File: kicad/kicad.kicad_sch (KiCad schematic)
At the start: 9 parts, among them SW101 PWR_SWITCH

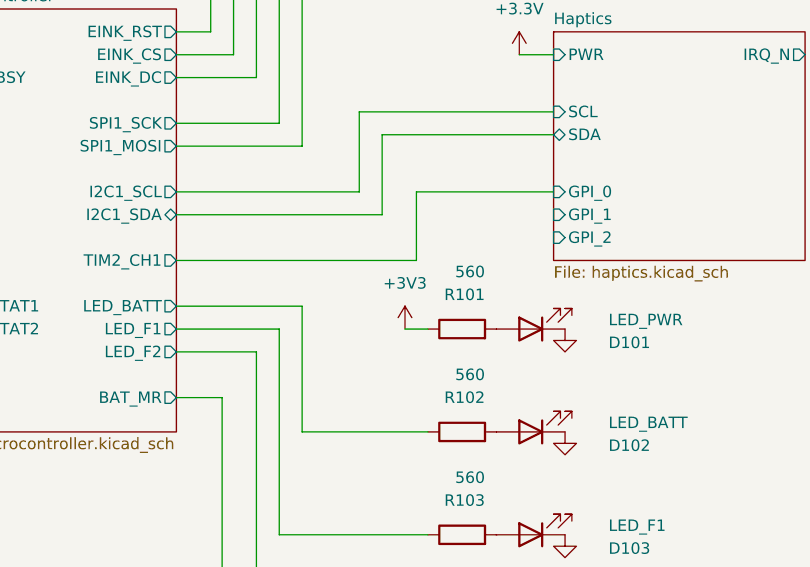
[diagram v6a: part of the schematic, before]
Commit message: PCB Trace progress
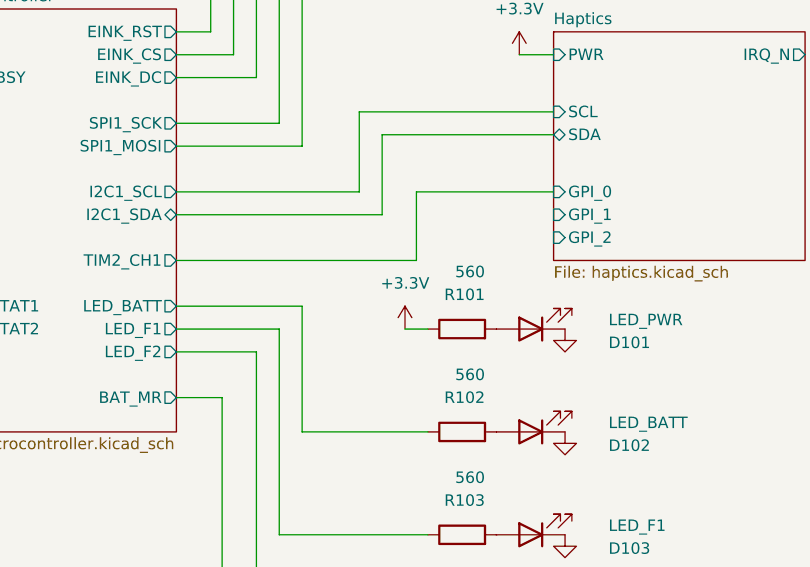
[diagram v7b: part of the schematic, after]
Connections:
- net +3V3 is gone; now on net +3.3V: R101.1
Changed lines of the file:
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@@
-	)
-	(symbol
-		(lib_id "power:+3V3")
-		(at 172.72 114.3 0)
-		(unit 1)
-		(exclude_from_sim no)
-		(in_bom yes)
-		(on_board yes)
-		(dnp no)
-		(fields_autoplaced yes)
-		(property "Reference" "#PWR0111"
-			(at 172.72 118.11 0)
-			(effects
-				(font
-					(size 1.27 1.27)
-				)
-				(hide yes)
-			)
-		)
-		(property "Value" "+3V3"
-			(at 172.72 109.22 0)
-			(effects
-				(font
-					(size 1.27 1.27)
-				)
-			)
-		)
-		(property "Footprint" ""
-			(at 172.72 114.3 0)
-			(effects
-				(font
-					(size 1.27 1.27)
-				)
-				(hide yes)
-			)
-		)
-		(property "Datasheet" ""
-			(at 172.72 114.3 0)
-			(effects
-				(font
-					(size 1.27 1.27)
-				)
-				(hide yes)
-			)
-		)
-		(property "Description" "Power symbol creates a global label with name \"+3V3\""
-			(at 172.72 114.3 0)
-			(effects
-				(font
-					(size 1.27 1.27)
-				)
-				(hide yes)
-			)
-		)
-		(pin "1"
-		)
-		(instances
-			(project "kicad"
-				(path "/97e37379-fec6-4f0d-82d9-4ea53516bb02"
-					(reference "#PWR0111")
-					(unit 1)
-				)
-			)
-		)
 	)
 	(symbol
@@
 					(unit 1)
 				)
+			)
+		)
+	)
+	(symbol
+		(lib_id "power:+3.3V")
+		(at 172.72 114.3 0)
+		(unit 1)
+		(exclude_from_sim no)
+		(in_bom yes)
+		(on_board yes)
+		(dnp no)
+		(fields_autoplaced yes)
+		(property "Reference" "#PWR0111"
+			(at 172.72 118.11 0)
+			(effects
+				(font
+					(size 1.27 1.27)
+				)
+				(hide yes)
+			)
+		)
+		(property "Value" "+3.3V"
+			(at 172.72 109.22 0)
+			(effects
+				(font
+					(size 1.27 1.27)
+				)
+			)
+		)
+		(property "Footprint" ""
+			(at 172.72 114.3 0)
+			(effects
+				(font
+					(size 1.27 1.27)
+				)
+				(hide yes)
+			)
+		)
+		(property "Datasheet" ""
+			(at 172.72 114.3 0)
+			(effects
+				(font
+					(size 1.27 1.27)
+				)
+				(hide yes)
+			)
+		)
+		(property "Description" "Power symbol creates a global label with name \"+3.3V\""
+			(at 172.72 114.3 0)
+			(effects
+				(font
+					(size 1.27 1.27)
+				)
+				(hide yes)
+			)
+		)
+		(pin "1"
+		)
+		(instances
+			(project "kicad"
+				(path "/97e37379-fec6-4f0d-82d9-4ea53516bb02"
+					(reference "#PWR0111")
+					(unit 1)
+				)

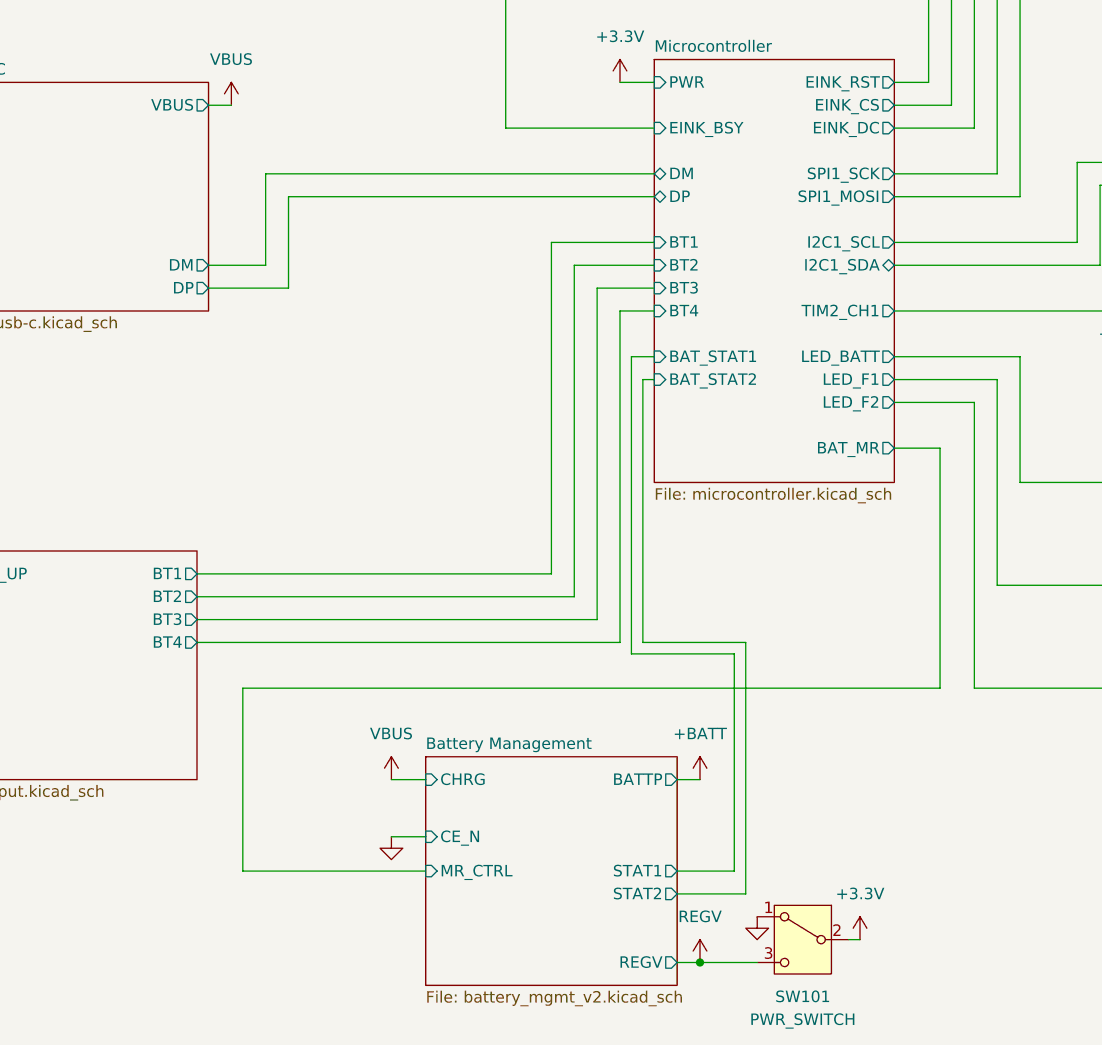
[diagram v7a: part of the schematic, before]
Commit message: Minor schematic fixes and PCB trace progress
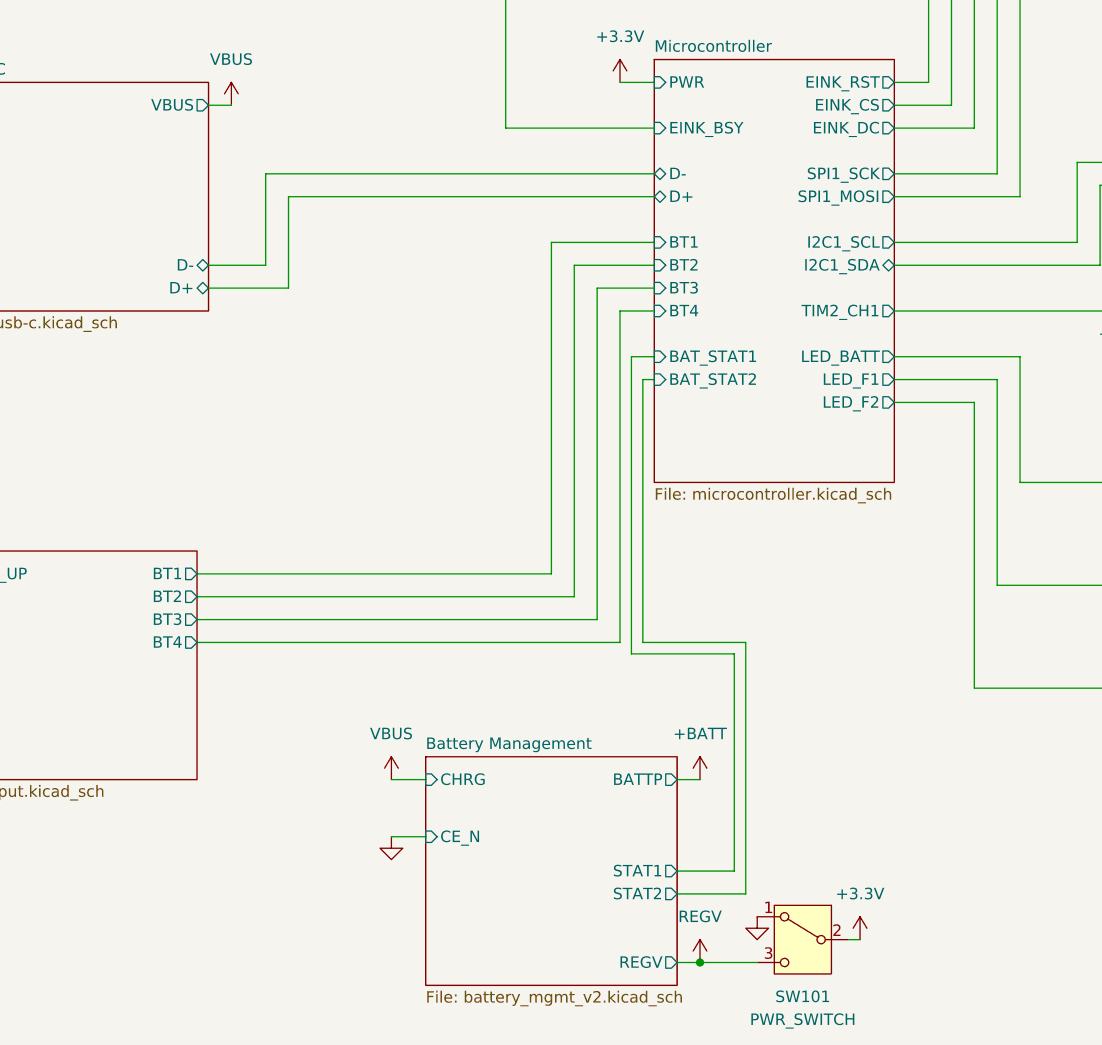
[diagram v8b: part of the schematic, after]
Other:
- sheet Battery Management ports: added none; removed MR_CTRL
- sheet Microcontroller ports: added D+, D-; removed BAT_MR, DM, DP
- sheet USB-C ports: added D+, D-; removed DM, DP
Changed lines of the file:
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@@
 	(wire
 		(pts
-			(xy 95.25 168.91) (xy 74.93 168.91)
-		)
-		(stroke
-			(width 0)
-			(type default)
-		)
-	)
-	(wire
-		(pts
 			(xy 151.13 44.45) (xy 163.83 44.45)
 		)
@@
 	(wire
 		(pts
-			(xy 74.93 168.91) (xy 74.93 148.59)
-		)
-		(stroke
-			(width 0)
-			(type default)
-		)
-	)
-	(wire
-		(pts
 			(xy 104.14 86.36) (xy 104.14 68.58)
 		)
@@
 	(wire
 		(pts
-			(xy 152.4 121.92) (xy 147.32 121.92)
-		)
-		(stroke
-			(width 0)
-			(type default)
-		)
-	)
-	(wire
-		(pts
 			(xy 120.65 86.36) (xy 104.14 86.36)
 		)
@@
 	(wire
 		(pts
-			(xy 152.4 148.59) (xy 152.4 121.92)
-		)
-		(stroke
-			(width 0)
-			(type default)
-		)
-	)
-	(wire
-		(pts
 			(xy 120.65 93.98) (xy 80.01 93.98)
 		)
@@
 	(wire
 		(pts
-			(xy 74.93 148.59) (xy 152.4 148.59)
-		)
-		(stroke
-			(width 0)
-			(type default)
-		)
-	)
-	(wire
-		(pts
 			(xy 170.18 92.71) (xy 170.18 101.6)
 		)
@@
 			)
 		)
-		(pin "DM" output
-			(at 71.12 101.6 0)
+		(pin "VBUS" output
+			(at 71.12 83.82 0)
 			(effects
 				(font
@@
 			)
 		)
-		(pin "DP" output
-			(at 71.12 104.14 0)
+		(pin "D-" bidirectional
+			(at 71.12 101.6 0)
 			(effects
 				(font
@@
 			)
 		)
-		(pin "VBUS" output
-			(at 71.12 83.82 0)
+		(pin "D+" bidirectional
+			(at 71.12 104.14 0)
 			(effects
 				(font
@@
 			)
 		)
-		(pin "DP" bidirectional
-			(at 120.65 93.98 180)
-			(effects
-				(font
-					(size 1.27 1.27)
-				)
-				(justify left)
-			)
-		)
-		(pin "DM" bidirectional
-			(at 120.65 91.44 180)
-			(effects
-				(font
-					(size 1.27 1.27)
-				)
-				(justify left)
-			)
-		)
 		(pin "I2C1_SCL" output
 			(at 147.32 99.06 0)
@@
 			)
 		)
-		(pin "BAT_MR" output
-			(at 147.32 121.92 0)
-			(effects
-				(font
-					(size 1.27 1.27)
-				)
-				(justify right)
-			)
-		)
 		(pin "LED_F1" output
 			(at 147.32 114.3 0)
@@
 			)
 		)
+		(pin "D-" bidirectional
+			(at 120.65 91.44 180)
+			(effects
+				(font
+					(size 1.27 1.27)
+				)
+				(justify left)
+			)
+		)
+		(pin "D+" bidirectional
+			(at 120.65 93.98 180)
+			(effects
+				(font
+					(size 1.27 1.27)
+				)
+				(justify left)
+			)
+		)
 		(instances
 			(project "kicad"
@@
 			)
 		)
-		(pin "MR_CTRL" input
-			(at 95.25 168.91 180)
-			(effects
-				(font
-					(size 1.27 1.27)
-				)
-				(justify left)
-			)
-		)
